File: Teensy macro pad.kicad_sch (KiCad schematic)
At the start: 22 parts, among them J1 Teensy pins GND-10, J2 Teensy pins +5V-11, SW0,0 CherryMX, SW0,1 CherryMX, SW0,2 CherryMX, SW0,3 CherryMX, SW0,4 CherryMX, SW1,0 CherryMX, SW1,1 CherryMX, SW1,2 CherryMX, SW1,3 CherryMX, SW1,4 CherryMX, SW2,0 CherryMX, SW2,1 CherryMX, SW2,2 CherryMX, SW2,3 CherryMX, SW2,4 CherryMX, SW3,0 CherryMX, SW3,1 CherryMX, SW3,2 CherryMX, SW3,3 CherryMX, SW3,4 CherryMX

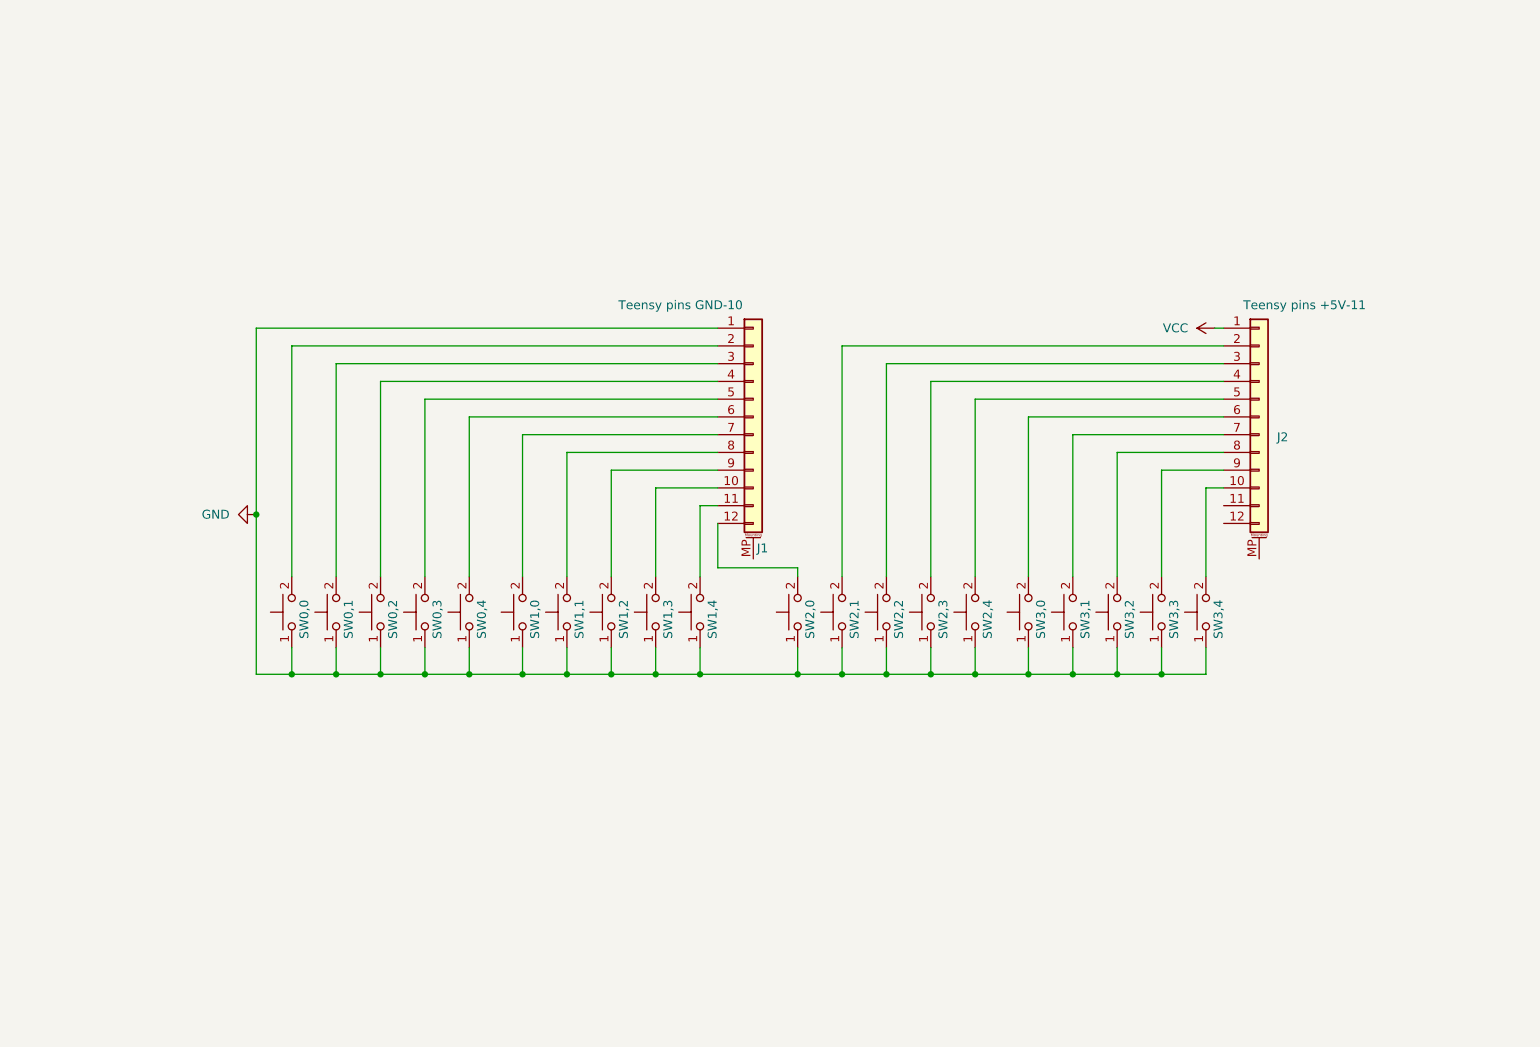
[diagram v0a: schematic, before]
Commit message: Switch to putting the chip on the board directly
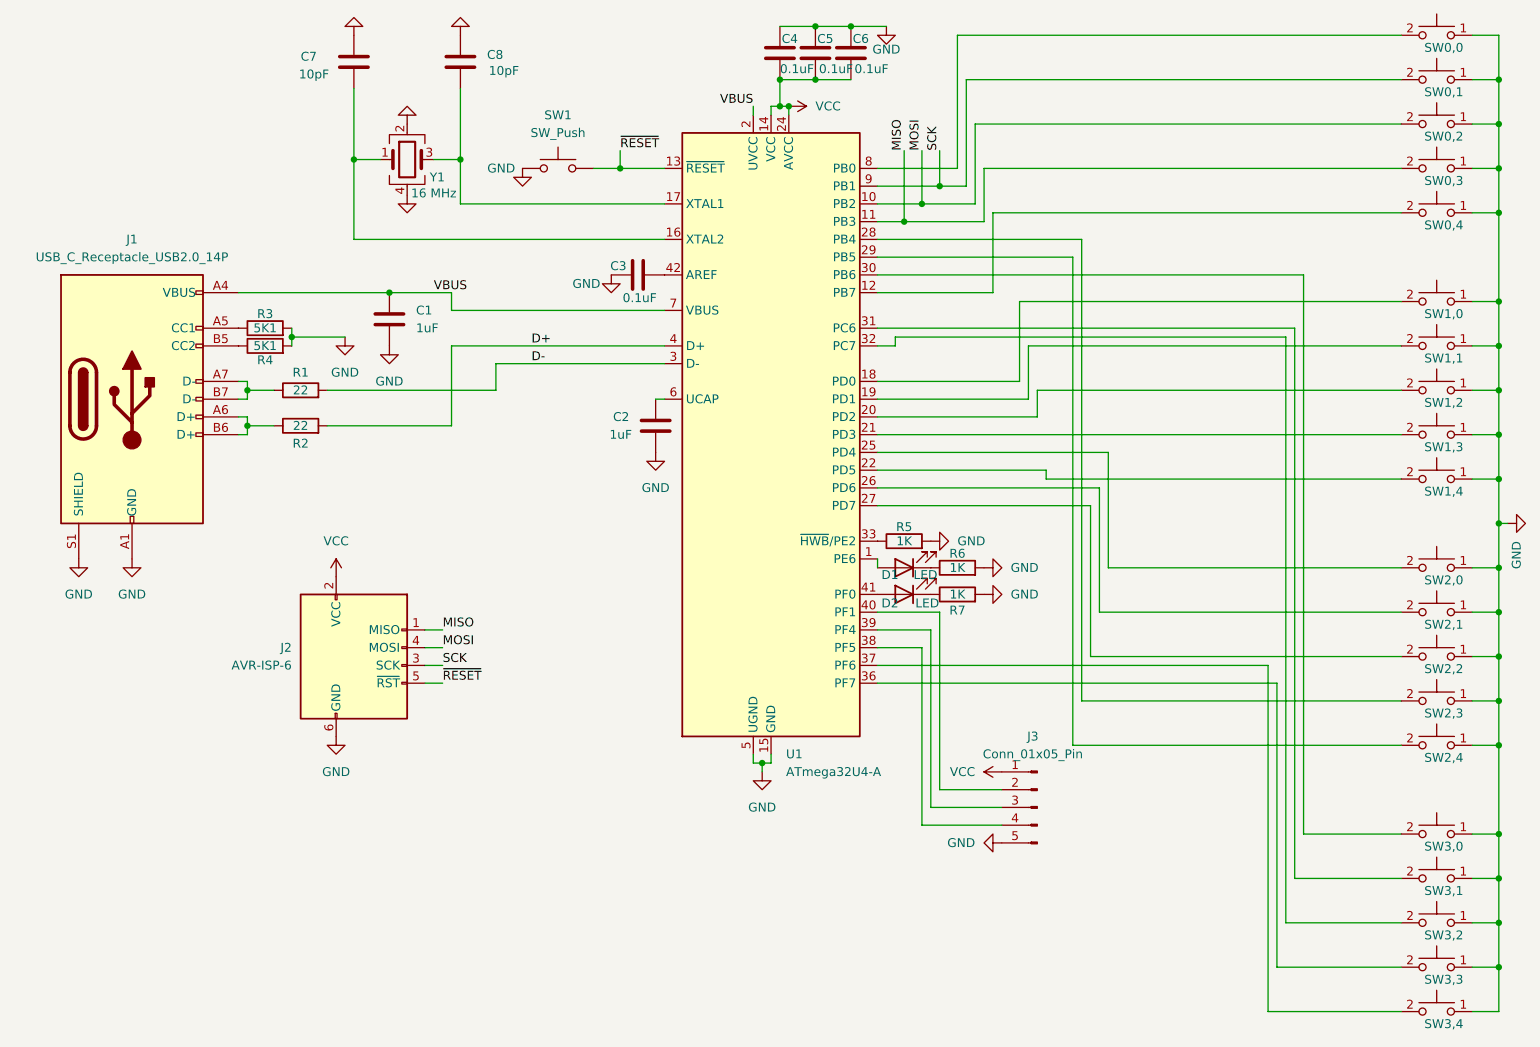
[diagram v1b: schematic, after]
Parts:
- removed J1: Teensy pins GND-10, Connector_PinSocket_2.54mm:PinSocket_1x12_P2.54mm_Vertical, symbol Connector_Generic_MountingPin:Conn_01x12_MountingPin
- removed J2: Teensy pins +5V-11, Connector_PinSocket_2.54mm:PinSocket_1x12_P2.54mm_Vertical, symbol Connector_Generic_MountingPin:Conn_01x12_MountingPin
- added C1, C2: 1uF, Capacitor_SMD:C_0805_2012Metric, symbol Device:C
- added C3, C4, C5, C6: 0.1uF, Capacitor_SMD:C_0805_2012Metric, symbol Device:C
- added C7, C8: 10pF, Capacitor_SMD:C_0805_2012Metric, symbol Device:C
- added D1, D2: LED, LED_THT:LED_D5.0mm, symbol Device:LED
- added J1: USB_C_Receptacle_USB2.0_14P, Connector_USB:USB_C_Receptacle_G-Switch_GT-USB-7010ASV, symbol Connector:USB_C_Receptacle_USB2.0_14P
- added J2: AVR-ISP-6, Connector_IDC:IDC-Header_2x03_P2.54mm_Vertical, symbol Connector:AVR-ISP-6
- added J3: Conn_01x05_Pin, Connector_PinHeader_2.54mm:PinHeader_1x05_P2.54mm_Vertical, symbol Connector:Conn_01x05_Pin
- added R1, R2: 22, Resistor_SMD:R_0805_2012Metric, symbol Device:R
- added R3, R4: 5K1, Resistor_SMD:R_0805_2012Metric, symbol Device:R
- added R5, R6, R7: 1K, Resistor_SMD:R_0805_2012Metric, symbol Device:R
- added SW1: SW_Push, Button_Switch_SMD:SW_Push_1P1T_XKB_TS-1187A, symbol Switch:SW_Push
- added U1: ATmega32U4-A, Package_QFP:TQFP-44_10x10mm_P0.8mm, symbol MCU_Microchip_ATmega:ATmega32U4-A
- added Y1: 16 MHz, Crystal:Crystal_SMD_3225-4Pin_3.2x2.5mm, symbol Device:Crystal_GND24
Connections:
- net GND: now also C1.2, C2.2, C3.1, C4.2, C5.2, C6.2, C7.1, C8.1, J1.A1 (GND), J1.A12 (GND), J1.B1 (GND), J1.B12 (GND), J1.S1 (SHIELD), J2.6 (GND), J3.5 (Pin_5), R3.2, R4.2, R5.2, R6.2, R7.2, SW1.1, U1.15 (GND), U1.23 (GND), U1.35 (GND), U1.43 (GND), U1.5 (UGND), Y1.2, Y1.4
- net VCC: now also C4.1, C5.1, C6.1, J2.2 (VCC), J3.1 (Pin_1), U1.14 (VCC), U1.24 (AVCC), U1.34 (VCC), U1.44 (AVCC)
- net at SW1,3.2: now also U1.21 (PD3)
- net at SW1,4.2: now also U1.22 (PD5)
- net at SW2,0.2: now also U1.25 (PD4)
- net at SW0,0.2: now also U1.8 (PB0)
- net SCK: now reaches SW0,1.2
- net SCK: now also J2.3 (SCK), U1.9 (PB1)
- net MOSI: now reaches SW0,2.2
- net MOSI: now also J2.4 (MOSI), U1.10 (PB2)
- net MISO: now reaches SW0,3.2
- net MISO: now also J2.1 (MISO), U1.11 (PB3)
- net at SW0,4.2: now also U1.12 (PB7)
- net at SW1,0.2: now also U1.18 (PD0)
- net at SW1,1.2: now also U1.19 (PD1)
- net at SW1,2.2: now also U1.20 (PD2)
- net at SW3,4.2: now also U1.37 (PF6)
- net at SW2,1.2: now also U1.26 (PD6)
- net at SW2,2.2: now also U1.27 (PD7)
- net at SW2,3.2: now also U1.28 (PB4)
- net at SW2,4.2: now also U1.29 (PB5)
- net at SW3,0.2: now also U1.30 (PB6)
- net at SW3,1.2: now also U1.31 (PC6)
- net at SW3,2.2: now also U1.32 (PC7)
- net at SW3,3.2: now also U1.36 (PF7)
- new net: C8.2, U1.17 (XTAL1), Y1.3
- new net: D1.2 (A), U1.1 (PE6)
- new net: C7.2, U1.16 (XTAL2), Y1.1
- new net: R5.1, U1.33 (~{HWB}/PE2)
- new net: J3.4 (Pin_4), U1.38 (PF5)
- new net: J3.3 (Pin_3), U1.39 (PF4)
- new net: J3.2 (Pin_2), U1.40 (PF1)
- new net: D2.2 (A), U1.41 (PF0)
- new net: C3.2, U1.42 (AREF)
- new net: C2.1, U1.6 (UCAP)
- new net: J1.A6 (D+), J1.B6 (D+), R2.1
- new net: J1.A5 (CC1), R3.1
- new net: D1.1 (K), R6.1
- new net: J1.B5 (CC2), R4.1
- new net: J1.A7 (D-), J1.B7 (D-), R1.1
- new net: D2.1 (K), R7.1
- new net D+: R2.2, U1.4 (D+)
- new net D-: R1.2, U1.3 (D-)
- new net VBUS: C1.1, J1.A4 (VBUS), J1.A9 (VBUS), J1.B4 (VBUS), J1.B9 (VBUS), U1.2 (UVCC), U1.7 (VBUS)
- new net ~{RESET}: J2.5 (~{RST}), SW1.2, U1.13 (~{RESET})
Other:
- moved on the sheet: SW0,0, SW0,1, SW0,2, SW0,3, SW0,4, SW1,0, SW1,1, SW1,2, SW1,3, SW1,4, SW2,0, SW2,1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

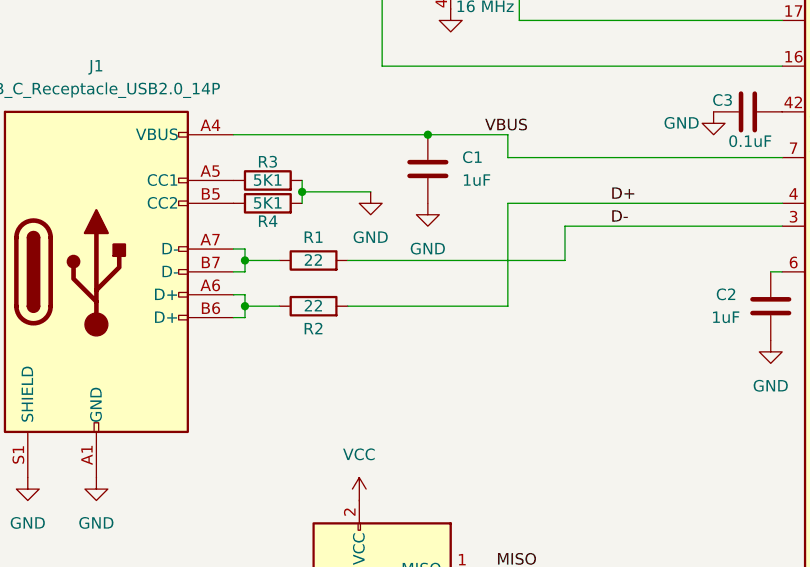
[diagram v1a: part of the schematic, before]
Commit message: Move decoupling capacitors to be one per VCC pin
Pages 5 and 6 of AN2519 [0] are particularly relevant here.

[0]: https://ww1.microchip.com/downloads/aemDocuments/documents/MCU08/ApplicationNotes/ApplicationNotes/AN2519-AVR-Microcontroller-Hardware-Design-Considerations-00002519B.pdf
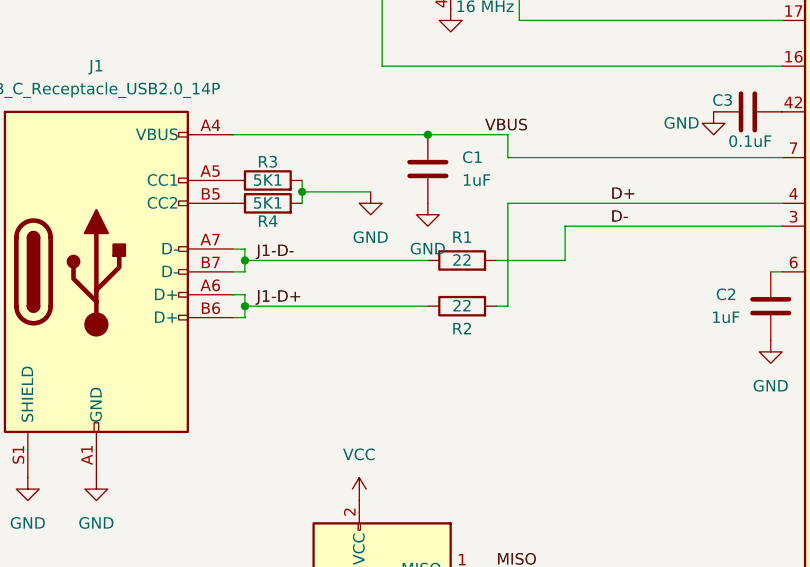
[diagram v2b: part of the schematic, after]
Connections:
- net J1-D+: now reaches J1.A6 (D+), J1.B6 (D+), R2.1
- net J1-D-: now reaches J1.A7 (D-), J1.B7 (D-), R1.1
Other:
- moved on the sheet: R1, R2
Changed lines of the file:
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@@
 	(wire
 		(pts
-			(xy 73.66 68.58) (xy 77.47 68.58)
-		)
-		(stroke
-			(width 0)
-			(type default)
-		)
-	)
-	(wire
-		(pts
 			(xy 252.73 151.13) (xy 252.73 144.78)
 		)
@@
 	(wire
 		(pts
-			(xy 73.66 73.66) (xy 77.47 73.66)
+			(xy 73.66 73.66) (xy 93.98 73.66)
 		)
 		(stroke
@@
 	(wire
 		(pts
-			(xy 85.09 73.66) (xy 102.87 73.66)
+			(xy 101.6 73.66) (xy 102.87 73.66)
 		)
 		(stroke
@@
 	(wire
 		(pts
-			(xy 85.09 68.58) (xy 109.22 68.58)
+			(xy 73.66 68.58) (xy 93.98 68.58)
+		)
+		(stroke
+			(width 0)
+			(type default)
+		)
+	)
+	(wire
+		(pts
+			(xy 101.6 68.58) (xy 109.22 68.58)
 		)
 		(stroke
@@
 		)
 	)
+	(label "J1-D+"
+		(at 74.93 73.66 0)
+		(effects
+			(font
+				(size 1.27 1.27)
+			)
+			(justify left bottom)
+		)
+	)
 	(label "~{RESET}"
 		(at 127 34.29 0)
@@
 		)
 	)
+	(label "J1-D-"
+		(at 74.93 68.58 0)
+		(effects
+			(font
+				(size 1.27 1.27)
+			)
+			(justify left bottom)
+		)
+	)
 	(label "D-"
 		(at 114.3 64.77 0)
@@
 	(symbol
 		(lib_id "Device:R")
-		(at 81.28 73.66 90)
+		(at 97.79 73.66 90)
 		(unit 1)
 		(exclude_from_sim no)
@@
 		(dnp no)
 		(property "Reference" "R2"
-			(at 81.28 76.2 90)
+			(at 97.79 76.2 90)
 			(effects
 				(font
@@
 		)
 		(property "Value" "22"
-			(at 81.28 73.66 90)
+			(at 97.79 73.66 90)
 			(effects
 				(font
@@
 		)
 		(property "Footprint" "Resistor_SMD:R_0805_2012Metric"
-			(at 81.28 75.438 90)
+			(at 97.79 75.438 90)
 			(effects
 				(font
@@
 		)
 		(property "Datasheet" "~"
-			(at 81.28 73.66 0)
+			(at 97.79 73.66 0)
 			(effects
 				(font
@@
 		)
 		(property "Description" "Resistor"
-			(at 81.28 73.66 0)
+			(at 97.79 73.66 0)
 			(effects
 				(font
@@
 	(symbol
 		(lib_id "Device:R")
-		(at 81.28 68.58 90)
+		(at 97.79 68.58 90)
 		(unit 1)
 		(exclude_from_sim no)
@@
 		(dnp no)
 		(property "Reference" "R1"
-			(at 81.28 66.04 90)
+			(at 97.79 66.04 90)
 			(effects
 				(font
@@
 		)
 		(property "Value" "22"
-			(at 81.28 68.58 90)
+			(at 97.79 68.58 90)
 			(effects
 				(font
@@
 		)
 		(property "Footprint" "Resistor_SMD:R_0805_2012Metric"
-			(at 81.28 70.358 90)
+			(at 97.79 70.358 90)
 			(effects
 				(font
@@
 		)
 		(property "Datasheet" "~"
-			(at 81.28 68.58 0)
+			(at 97.79 68.58 0)
 			(effects
 				(font
@@
 		)
 		(property "Description" "Resistor"
-			(at 81.28 68.58 0)
+			(at 97.79 68.58 0)
 			(effects
 				(font

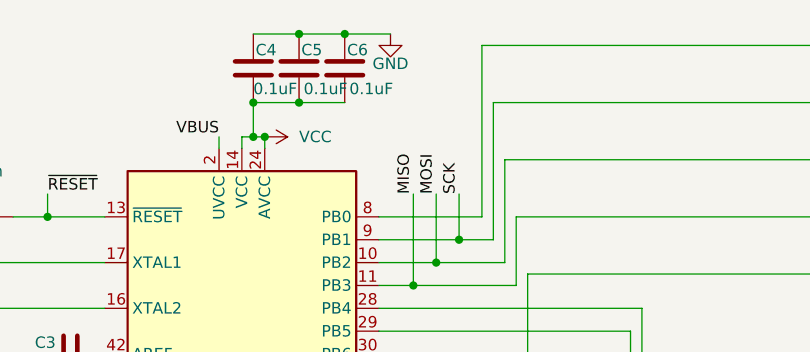
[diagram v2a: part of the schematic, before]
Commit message: Add a decoupling capacitor to VCC pin 44
This isn't on the Teensy, but AN2519 is quite clear that "For devices
with multiple pairs of power and ground pins, it is essential that there
is a decoupling capacitor for every pair of pins."
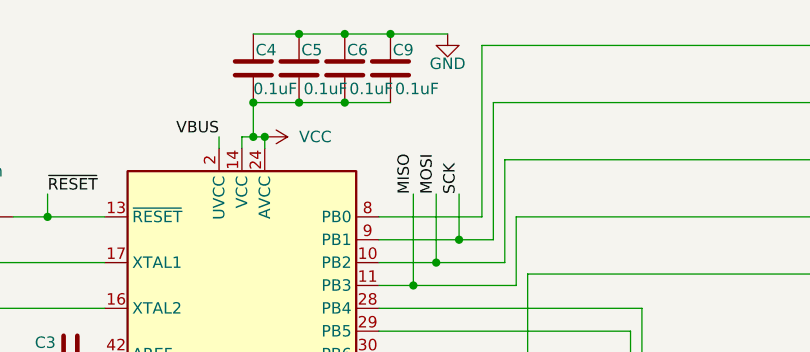
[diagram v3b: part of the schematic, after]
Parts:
- added C9: 0.1uF, Capacitor_SMD:C_0805_2012Metric, symbol Device:C
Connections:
- net GND: now also C9.2
- net VCC: now also C9.1
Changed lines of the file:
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@@
 	)
 	(junction
+		(at 160.02 24.13)
+		(diameter 0)
+		(color 0 0 0 0)
+	)
+	(junction
 		(at 252.73 36.83)
 		(diameter 0)
@@
 	)
 	(junction
+		(at 165.1 16.51)
+		(diameter 0)
+		(color 0 0 0 0)
+	)
+	(junction
 		(at 93.98 54.61)
 		(diameter 0)
@@
 	(wire
 		(pts
+			(xy 165.1 16.51) (xy 171.45 16.51)
+		)
+		(stroke
+			(width 0)
+			(type default)
+		)
+	)
+	(wire
+		(pts
 			(xy 147.32 121.92) (xy 147.32 123.19)
 		)
@@
 	(wire
 		(pts
+			(xy 160.02 24.13) (xy 165.1 24.13)
+		)
+		(stroke
+			(width 0)
+			(type default)
+		)
+	)
+	(wire
+		(pts
 			(xy 154.94 24.13) (xy 160.02 24.13)
 		)
@@
 	(symbol
 		(lib_id "power:GND")
-		(at 165.1 16.51 0)
+		(at 171.45 16.51 0)
 		(unit 1)
 		(exclude_from_sim no)
@@
 		(dnp no)
 		(property "Reference" "#PWR011"
-			(at 165.1 22.86 0)
+			(at 171.45 22.86 0)
 			(effects
 				(font
@@
 		)
 		(property "Value" "GND"
-			(at 165.1 19.812 0)
+			(at 171.45 19.812 0)
 			(effects
 				(font
@@
 		)
 		(property "Footprint" ""
-			(at 165.1 16.51 0)
+			(at 171.45 16.51 0)
 			(effects
 				(font
@@
 		)
 		(property "Datasheet" ""
-			(at 165.1 16.51 0)
+			(at 171.45 16.51 0)
 			(effects
 				(font
@@
 		)
 		(property "Description" "Power symbol creates a global label with name \"GND\" , ground"
-			(at 165.1 16.51 0)
+			(at 171.45 16.51 0)
 			(effects
 				(font
@@
 					(unit 1)
 				)
+			)
+		)
+	)
+	(symbol
+		(lib_id "Device:C")
+		(at 165.1 20.32 180)
+		(unit 1)
+		(exclude_from_sim no)
+		(in_bom yes)
+		(on_board yes)
+		(dnp no)
+		(property "Reference" "C9"
+			(at 165.354 18.288 0)
+			(effects
+				(font
+					(size 1.27 1.27)
+				)
+				(justify right)
+			)
+		)
+		(property "Value" "0.1uF"
+			(at 165.608 22.606 0)
+			(effects
+				(font
+					(size 1.27 1.27)
+				)
+				(justify right)
+			)
+		)
+		(property "Footprint" "Capacitor_SMD:C_0805_2012Metric"
+			(at 164.1348 16.51 0)
+			(effects
+				(font
+					(size 1.27 1.27)
+				)
+				(hide yes)
+			)
+		)
+		(property "Datasheet" "~"
+			(at 165.1 20.32 0)
+			(effects
+				(font
+					(size 1.27 1.27)
+				)
+				(hide yes)
+			)
+		)
+		(property "Description" "Unpolarized capacitor"
+			(at 165.1 20.32 0)
+			(effects
+				(font
+					(size 1.27 1.27)
+				)
+				(hide yes)
+			)
+		)
+		(pin "2"
+		)
+		(pin "1"
+		)
+		(instances
+			(project "Teensy macro pad"
+				(path "/bcf4c563-ed90-4192-81fd-782593c0996d"
+					(reference "C9")
+					(unit 1)
+				)

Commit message: Change and move USB-C connector footprint
The old footprint was causing DRC errors (due to pads being too close to
its holes). Replace it with the one Matthew recommends
(...TYPE-C-31-M-12) and also move it so the edge of the connector
overhangs the board edge to make it easier to put the board in a case or
something.
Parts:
- J1: footprint Connector_USB:USB_C_Receptacle_G-Switch_GT-USB-7010ASV -> Connector_USB:USB_C_Receptacle_HRO_TYPE-C-31-M-12
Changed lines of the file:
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@@
 			)
 		)
-		(property "Footprint" "Connector_USB:USB_C_Receptacle_G-Switch_GT-USB-7010ASV"
+		(property "Footprint" "Connector_USB:USB_C_Receptacle_HRO_TYPE-C-31-M-12"
 			(at 60.96 69.85 0)
 			(effects

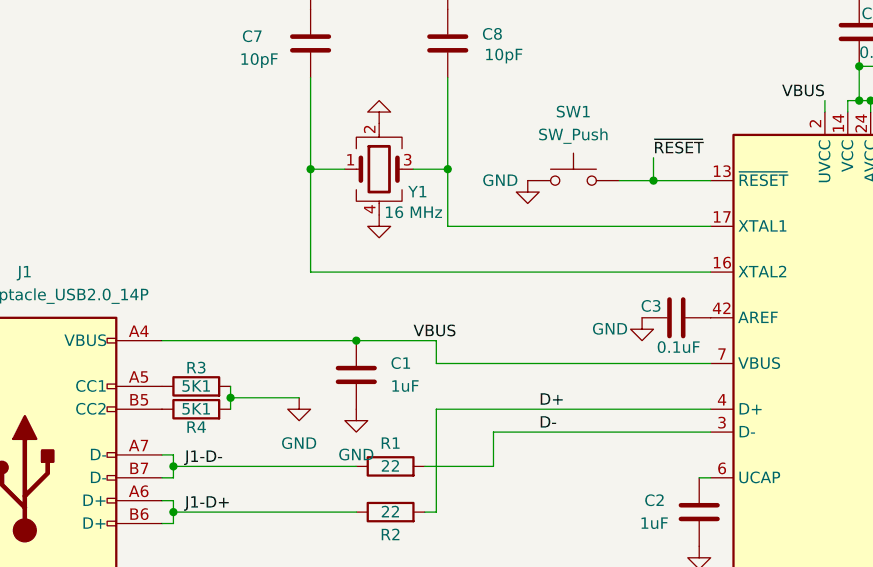
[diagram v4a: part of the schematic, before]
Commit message: Add test points for VBUS, XTAL1, and XTAL2
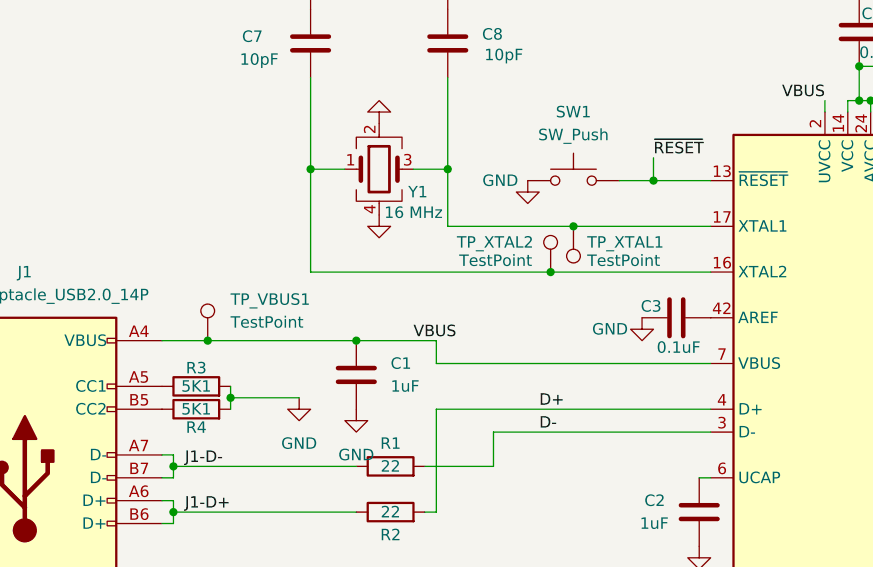
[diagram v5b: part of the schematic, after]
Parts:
- added TP_VBUS1, TP_XTAL1, TP_XTAL2: TestPoint, TestPoint:TestPoint_Pad_D2.0mm, symbol Connector:TestPoint
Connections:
- net VBUS: now also TP_VBUS1.1
- net at C8.2, U1.17 (XTAL1), Y1.3: now also TP_XTAL1.1
- net at C7.2, U1.16 (XTAL2), Y1.1: now also TP_XTAL2.1
